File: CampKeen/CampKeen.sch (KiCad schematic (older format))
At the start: 41 parts, among them P1 Digital, P10 CONN_01X01, P11 CONN_01X01, P12 CONN_01X01, P13 CONN_01X01, P2 Power, P3 Analog, P4 Analog, P5 PWM, P6 PWM, P7 Communication, P8 CONN_01X01, P9 CONN_01X01

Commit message: 0.1 version needs to have a power subsystem designed for the AVR and the PCB layout done.
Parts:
- removed Q? (x8): 2N7002, Package_TO_SOT_SMD:SOT-23, symbol Transistor_FET:2N7002
- removed R? (x8): R, symbol Device:R
- added BR1: DF04M, SamacSys_Parts:DIP825W58P510L828H330Q4N, symbol SamacSys_Parts:DF04M
- added C1, C6, C7: 0.1uF, Capacitor_THT:C_Disc_D7.5mm_W5.0mm_P5.00mm, symbol Device:C
- added C10: 1000uF, Capacitor_THT:C_Disc_D7.5mm_W5.0mm_P5.00mm, symbol Device:C
- added C11: 2.2uF, Capacitor_THT:CP_Radial_D4.0mm_P2.00mm, symbol Device:CP
- added C12: 10nF, Capacitor_THT:C_Disc_D7.5mm_W5.0mm_P5.00mm, symbol Device:C
- added C2, C3, C4, C5: 1uF, Capacitor_THT:CP_Radial_D4.0mm_P2.00mm, symbol Device:CP
- added C8: 68uF, Capacitor_THT:CP_Radial_D4.0mm_P2.00mm, symbol Device:CP
- added C9: 120uF, Capacitor_THT:CP_Radial_D4.0mm_P2.00mm, symbol Device:CP
- added D1, D2: 1N5817, SamacSys_Parts:DIOAD1414W86L464D238, symbol SamacSys_Parts:1N5817
- added IC2: TL071CP, SamacSys_Parts:DIP794W53P254L959H508Q8N, symbol SamacSys_Parts:TL071CP
- added IC3: LM2597MX-5.0_NOPB, SamacSys_Parts:SOIC127P600X175-8N, symbol SamacSys_Parts:LM2597MX-5.0_NOPB
- added J1: Tanks, SamacSys_Parts:1727751, symbol SamacSys_Parts:1727751
- added J10: VAC, TerminalBlock_Phoenix:TerminalBlock_Phoenix_MKDS-1,5-2-5.08_1x02_P5.08mm_Horizontal, symbol Connector:Screw_Terminal_01x02
- added J2, J5: IO, SamacSys_Parts:1727751, symbol SamacSys_Parts:1727751
- added J3: Temps, SamacSys_Parts:1727751, symbol SamacSys_Parts:1727751
- added J4: Vin, TerminalBlock_Phoenix:TerminalBlock_Phoenix_MKDS-1,5-2-5.08_1x02_P5.08mm_Horizontal, symbol Connector:Screw_Terminal_01x02
- added J6: GenEnclosure, Connector_PinSocket_2.54mm:PinSocket_1x08_P2.54mm_Vertical, symbol Connector_Generic:Conn_01x08
- added J7: GenHeadL, Connector_PinSocket_2.54mm:PinSocket_1x08_P2.54mm_Vertical, symbol Connector_Generic:Conn_01x08
- added J8: GenHeadR, Connector_PinSocket_2.54mm:PinSocket_1x08_P2.54mm_Vertical, symbol Connector_Generic:Conn_01x08
- added J9: CAC, TerminalBlock_Phoenix:TerminalBlock_Phoenix_MKDS-1,5-2-5.08_1x02_P5.08mm_Horizontal, symbol Connector:Screw_Terminal_01x02
- added K1, K2, K3: DIP05-1A72-12L, SamacSys_Parts:DIP051A7212L, symbol SamacSys_Parts:DIP05-1A72-12L
- added L1: 100mH, Inductor_THT:L_Axial_L9.5mm_D4.0mm_P15.24mm_Horizontal_Fastron_SMCC, symbol Device:L
- added Q1, Q16, Q24, Q6: BC547, Package_TO_SOT_THT:TO-92_Inline, symbol Transistor_BJT:BC547
- added Q10, Q11, Q12, Q13, Q19, Q2, Q20, Q21, Q22, Q23, Q3, Q4, Q5, Q7, Q8, Q9: 2N7000, Package_TO_SOT_THT:TO-92_Inline, symbol Transistor_FET:2N7000
- added Q15, Q17, Q18, Q25: IRF510, SamacSys_Parts:TO254P465X1024X2050-3P, symbol SamacSys_Parts:IRF510
- added R1, R2, R32, R35, R36, R52: 47k, Resistor_THT:R_Axial_DIN0207_L6.3mm_D2.5mm_P7.62mm_Horizontal, symbol Device:R
- added R14, R8: 47K, Resistor_THT:R_Axial_DIN0207_L6.3mm_D2.5mm_P7.62mm_Horizontal, symbol Device:R
- added R15, R16, R3, R33, R34, R4, R47, R48: R, Resistor_THT:R_Axial_DIN0207_L6.3mm_D2.5mm_P7.62mm_Horizontal, symbol Device:R
- added R17, R18, R19, R20, R21, R22, R23, R24, R25, R26, R27, R28, R29, R30, R37, R38, R39, R40, R41, R42, R43, R44, R45, R46: 100k, Resistor_THT:R_Axial_DIN0207_L6.3mm_D2.5mm_P7.62mm_Horizontal, symbol Device:R
- added R49: 10k, Resistor_THT:R_Axial_DIN0207_L6.3mm_D2.5mm_P7.62mm_Horizontal, symbol Device:R
- added R50: 33, Resistor_THT:R_Axial_DIN0207_L6.3mm_D2.5mm_P7.62mm_Horizontal, symbol Device:R
- added R51: 1M, Resistor_THT:R_Axial_DIN0207_L6.3mm_D2.5mm_P7.62mm_Horizontal, symbol Device:R
- added R53, R54: 50, Resistor_THT:R_Axial_DIN0207_L6.3mm_D2.5mm_P7.62mm_Horizontal, symbol Device:R
- added RV1: 500K, Potentiometer_THT:Potentiometer_Bourns_3296W_Vertical, symbol Device:R_POT_US
- added RV10, RV2, RV3, RV4, RV5, RV6, RV7, RV8, RV9: 20k, Potentiometer_THT:Potentiometer_Bourns_3296W_Vertical, symbol Device:R_POT_US
- added RV11: 1M, Potentiometer_THT:Potentiometer_Bourns_3296W_Vertical, symbol Device:R_POT_US
- added U2: TanksVS, SamacSys_Parts:BK_HTC-15M, symbol SamacSys_Parts:BK_HTC-15M
- added U3: MAX232, Package_DIP:DIP-16_W7.62mm_LongPads, symbol Interface_UART:MAX232
- added U4: VS, SamacSys_Parts:BK_HTC-15M, symbol SamacSys_Parts:BK_HTC-15M
- added U5: LPGVS, SamacSys_Parts:BK_HTC-15M, symbol SamacSys_Parts:BK_HTC-15M
- added U6: VAC, SamacSys_Parts:BK_HTC-15M, symbol SamacSys_Parts:BK_HTC-15M
- IC1: renamed from IC?; footprint SOIC127P1032X265-16N -> SamacSys_Parts:SOIC127P1032X265-16N
- Q14: renamed from Q?; footprint TO254P465X1024X2050-3P -> SamacSys_Parts:TO254P465X1024X2050-3P
- R10, R11, R12, R13, R7, R9: renamed from R?; value R -> 100k; footprint (none) -> Resistor_THT:R_Axial_DIN0207_L6.3mm_D2.5mm_P7.62mm_Horizontal
- R31: renamed from R?; value R -> 47k; footprint (none) -> Resistor_THT:R_Axial_DIN0207_L6.3mm_D2.5mm_P7.62mm_Horizontal
- R5, R6: renamed from R?; value R -> 100K; footprint (none) -> Resistor_THT:R_Axial_DIN0207_L6.3mm_D2.5mm_P7.62mm_Horizontal
- U1: renamed from U?; footprint S8411-45R_1 -> SamacSys_Parts:S8411-45R_1
- renumbered P2 to P1, P3 to P2, P4 to P3, P1 to P4
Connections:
- net labels added: +12V, +5P, BathroomPumpLED, BathroomWPS, CLK, CityWaterValveSense, D22, D43, D45, D47, D49, G1-2, G1-4, G3-4, G4-4, GWT12V, GenFuel, KitchenPumpLED, KitchenWPS, LCDBackLight, LCDBacklight, LCDBacklightOut, LPG, LPGSensor, MISO, MOSI, S1-2, S1-4, S3-4, S4-4, ST12V, WarningAlarm, WarningLED, Water, WaterPumpOnSense, d24, d26, d28
- wire segments 177 -> 709
- no-connect marks 7 -> 43
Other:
- moved on the sheet: IC1, Q14, R10, R11, R12, R13, R31, R5, R6, R7, R9, U1

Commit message: 0.1 i think it's ready to be sent off to be fabbed
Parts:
- removed Q19, Q21: 2N7000, Package_TO_SOT_THT:TO-92_Inline, symbol Transistor_FET:2N7000
- removed R37, R38, R41, R42: 100k, Resistor_THT:R_Axial_DIN0207_L6.3mm_D2.5mm_P7.62mm_Horizontal, symbol Device:R
- removed RV2, RV3, RV4, RV5, RV6, RV7, RV8, RV9: 20k, Potentiometer_THT:Potentiometer_Bourns_3296W_Vertical, symbol Device:R_POT_US
- added IC4: TL071CP, SamacSys_Parts:DIP794W53P254L959H508Q8N, symbol SamacSys_Parts:TL071CP
- added J12: IO1, SamacSys_Parts:1727751, symbol SamacSys_Parts:1727751
- added J2: 5VJumper, Connector_PinHeader_2.54mm:PinHeader_1x02_P2.54mm_Vertical, symbol Connector_Generic:Conn_01x02
- added Q20, Q22, Q26, Q27, Q32, Q35: IRF510, SamacSys_Parts:TO254P465X1024X2050-3P, symbol SamacSys_Parts:IRF510
- added Q28, Q29, Q30, Q31, Q33, Q34: 2N7000, Package_TO_SOT_THT:TO-92_Inline, symbol Transistor_FET:2N7000
- added R18: 47K, Resistor_THT:R_Axial_DIN0207_L6.3mm_D2.5mm_P7.62mm_Horizontal, symbol Device:R
- added R44, R45, R48, R49, R63, R68: 47k, Resistor_THT:R_Axial_DIN0207_L6.3mm_D2.5mm_P7.62mm_Horizontal, symbol Device:R
- added R56, R57, R58, R59, R60, R61, R62, R64, R65, R66, R67, R69: 100k, Resistor_THT:R_Axial_DIN0207_L6.3mm_D2.5mm_P7.62mm_Horizontal, symbol Device:R
- added R70, R71, R72, R73, R74, R75, R76, R77: 10k, Resistor_THT:R_Axial_DIN0207_L6.3mm_D2.5mm_P7.62mm_Horizontal, symbol Device:R
- C1: renamed from C6; footprint Capacitor_THT:C_Disc_D7.5mm_W5.0mm_P5.00mm -> Capacitor_THT:C_Rect_L9.0mm_W3.6mm_P7.50mm_MKT
- C10: renamed from C3; footprint Capacitor_THT:CP_Radial_D4.0mm_P2.00mm -> Capacitor_THT:CP_Radial_D5.0mm_P2.50mm
- C11: renamed from C4; footprint Capacitor_THT:CP_Radial_D4.0mm_P2.00mm -> Capacitor_THT:CP_Radial_D5.0mm_P2.50mm
- C12: renamed from C5; footprint Capacitor_THT:CP_Radial_D4.0mm_P2.00mm -> Capacitor_THT:CP_Radial_D5.0mm_P2.50mm
- C2: renamed from C7; footprint Capacitor_THT:C_Disc_D7.5mm_W5.0mm_P5.00mm -> Capacitor_THT:C_Rect_L9.0mm_W3.6mm_P7.50mm_MKT
- C3: renamed from C8; footprint Capacitor_THT:CP_Radial_D4.0mm_P2.00mm -> Capacitor_THT:CP_Radial_D5.0mm_P2.50mm
- C4: renamed from C9; footprint Capacitor_THT:CP_Radial_D4.0mm_P2.00mm -> Capacitor_THT:CP_Radial_D8.0mm_P5.00mm
- C5: renamed from C1; footprint Capacitor_THT:C_Disc_D7.5mm_W5.0mm_P5.00mm -> Capacitor_THT:C_Rect_L9.0mm_W3.6mm_P7.50mm_MKT
- C6: renamed from C10; footprint Capacitor_THT:C_Disc_D7.5mm_W5.0mm_P5.00mm -> Capacitor_THT:C_Rect_L9.0mm_W3.6mm_P7.50mm_MKT
- C9: renamed from C2; footprint Capacitor_THT:CP_Radial_D4.0mm_P2.00mm -> Capacitor_THT:CP_Radial_D5.0mm_P2.50mm
- J7: renamed from J5; value IO -> IO1
- R41: renamed from R53; value 50 -> 47
- R43: renamed from R54; value 50 -> 47
- renumbered C11 to C7, C12 to C8, IC3 to IC1, IC1 to IC2, IC2 to IC3, J4 to J1, J7 to J10, J8 to J11, J9 to J4, J1 to J5, J10 to J6, J2 to J8, J6 to J9, U5 to LPWater1, U4 to Main1, Q25 to Q12, Q12 to Q13, Q13 to Q14, Q16 to Q15, Q14 to Q16, Q15 to Q17, Q17 to Q18, Q18 to Q19, Q20 to Q21, Q22 to Q23, Q23 to Q24, Q24 to Q25, R49 to R1, R9 to R10, R51 to R11, R10 to R12, R50 to R13, R11 to R14, R12 to R15, R13 to R16, R14 to R17, R15 to R19, R1 to R2, R16 to R20, R17 to R21, R18 to R22, R19 to R23, R20 to R24, R21 to R25, R22 to R26, R23 to R27, R24 to R28, R25 to R29, R2 to R3, R26 to R30, R52 to R31, R27 to R32, R28 to R33, R29 to R34, R30 to R35, R33 to R36, R34 to R37, R31 to R38, R32 to R39, R3 to R4, R35 to R40, R36 to R42, R39 to R46, R40 to R47, R4 to R5, R43 to R50, R44 to R51, R45 to R52, R46 to R53, R47 to R54, R48 to R55, R5 to R6, R6 to R7, R7 to R8, R8 to R9, U1 to RTCBattery1, RV11 to RV10, RV10 to RV11, RV1 to RV9, U2 to Tanks1, U3 to U5, U6 to VACFuse1
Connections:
- net +5P: now also J2.1 (Pin_1)
- net +5V: now also IC4.7 (VCC+), J2.2 (Pin_2), Q28.3 (D), Q29.3 (D), Q30.3 (D), Q31.3 (D), Q33.3 (D), Q34.3 (D)
- net 10(**): now also Q28.1 (S), R57.1
- net 11(**): now also Q27.1, R49.1
- net 12(**): now also Q26.1, R48.1
- net 13(**): now also Q22.1, R45.1
- net 24: now also Q35.1, R68.1
- net 37: now also Q32.1, R63.1
- net 41: now also Q20.1, R44.1
- net 5(**): now also Q34.1 (S), R69.1
- net 6(**): now also Q33.1 (S), R66.1
- net 7(**): now also Q31.1 (S), R64.1
- net 8(**): now also Q30.1 (S), R61.1
- net 9(**): now also Q29.1 (S), R59.1
- net A10: now also R76.2
- net A11: now also IC4.2 (IN-), IC4.6 (OUT), R18.2; no longer R11.1, RV10.2
- net A14: now also J12.2
- net A15: now also J12.1
- net A3: now also R70.2
- net A4: now also R71.2
- net A5: now also R72.2
- net A6: now also R73.2
- net A7: now also R74.2
- net A8: now also R77.2
- net A9: now also R75.2
- net GND: now also IC4.4 (VCC-), Q20.3, Q22.3, Q26.3, Q27.3, Q32.3, Q35.3, R18.1, R44.2, R45.2, R48.2, R49.2, R56.2, R57.2, R58.2, R59.2, R60.2, R61.2, R62.2, R63.2, R64.2, R65.2, R66.2, R67.2, R68.2, R69.2, R70.1, R71.1, R72.1, R73.1, R74.1, R75.1, R76.1, R77.1
- net at J8.10: now also Q35.2
- net at J8.12: now also Q32.2
- net 22 renamed AlarmReset
- new net: IC4.3 (IN+), R11.1, RV10.2
- new net: J12.4, Q22.2
- new net: J12.10, Q31.2 (G), R62.1
- new net: J12.11, Q30.2 (G), R60.1
- new net: J12.12, Q29.2 (G), R58.1
- new net: J12.3, Q20.2
- new net: J12.5, Q26.2
- new net: J12.6, Q27.2
- new net: J12.7, Q28.2 (G), R56.1
- new net: J12.8, Q34.2 (G), R67.1
- new net: J12.9, Q33.2 (G), R65.1
- no-connect marks 43 -> 38
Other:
- moved on the sheet: BR1, C7, C8, J6, R11, RV10, VACFuse1

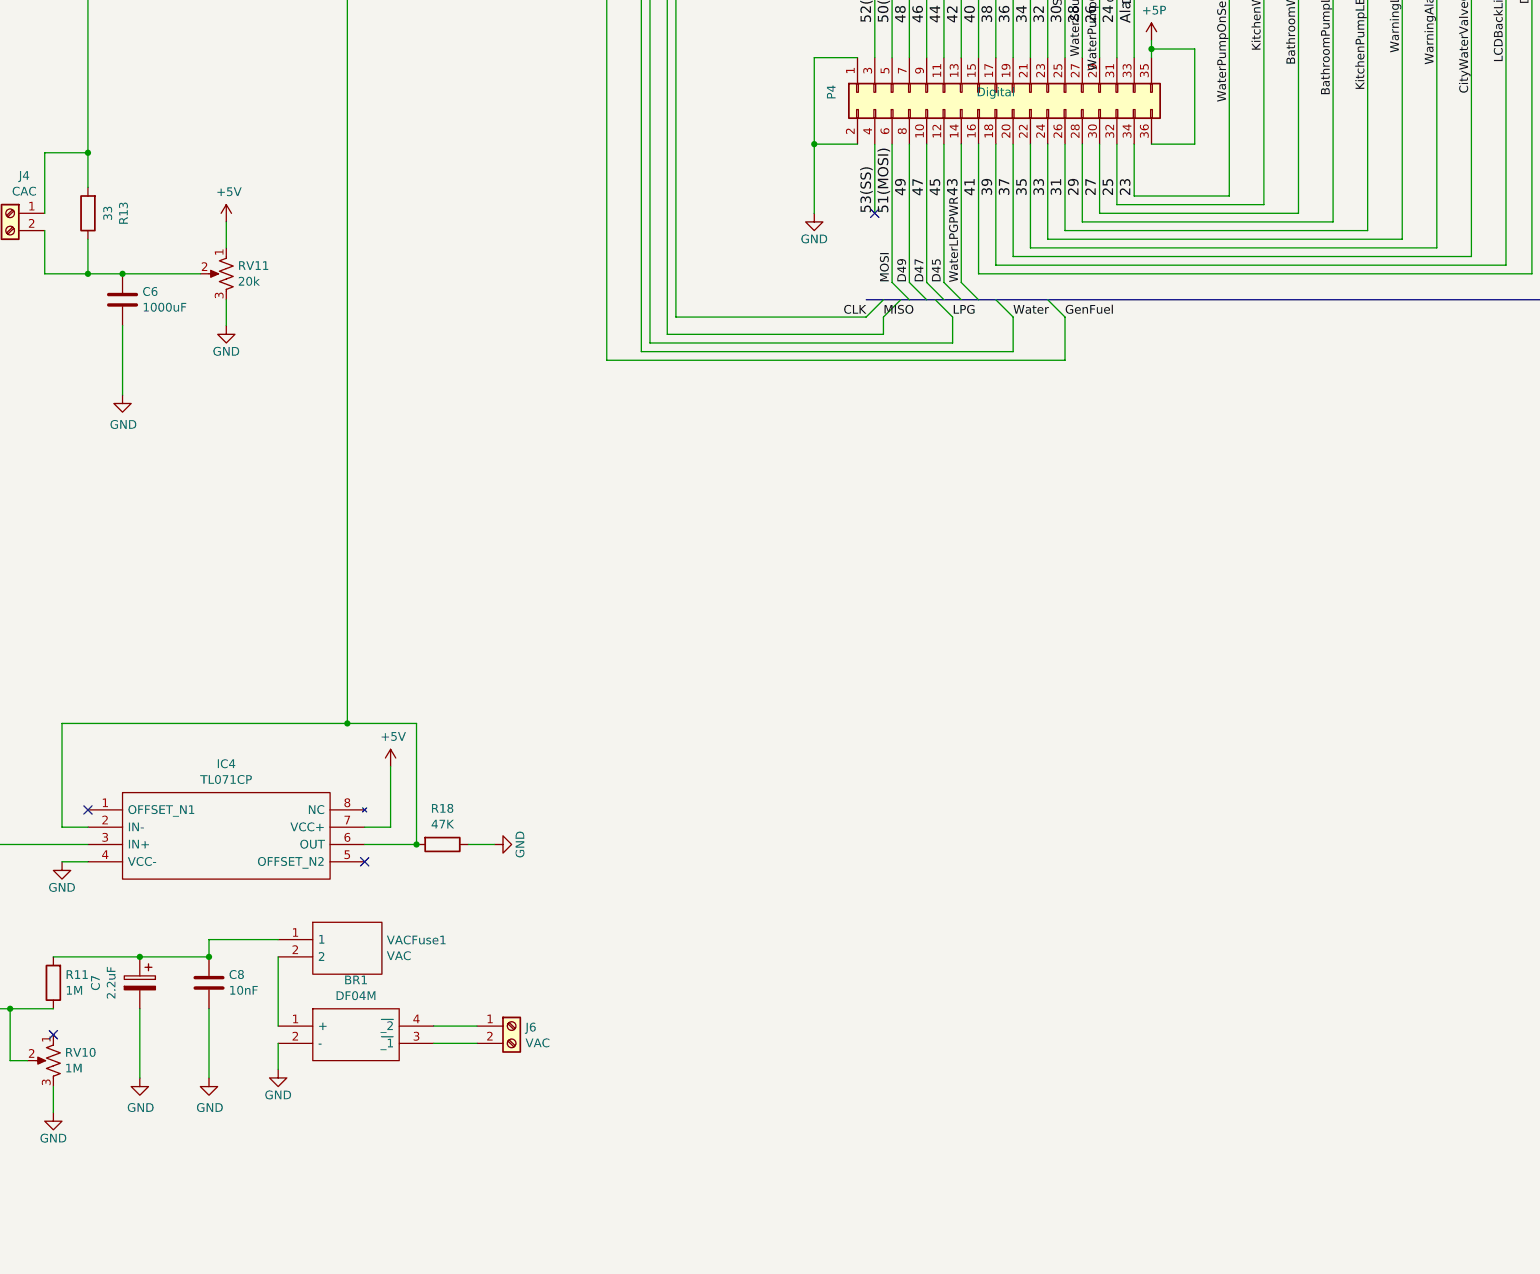
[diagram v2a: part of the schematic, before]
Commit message: WIP that needs to go in it's own branch. it has a few updates like putting the VAC transformer on board and a better voltage reference for the AC current. that still isn't done as it needs a buffer.
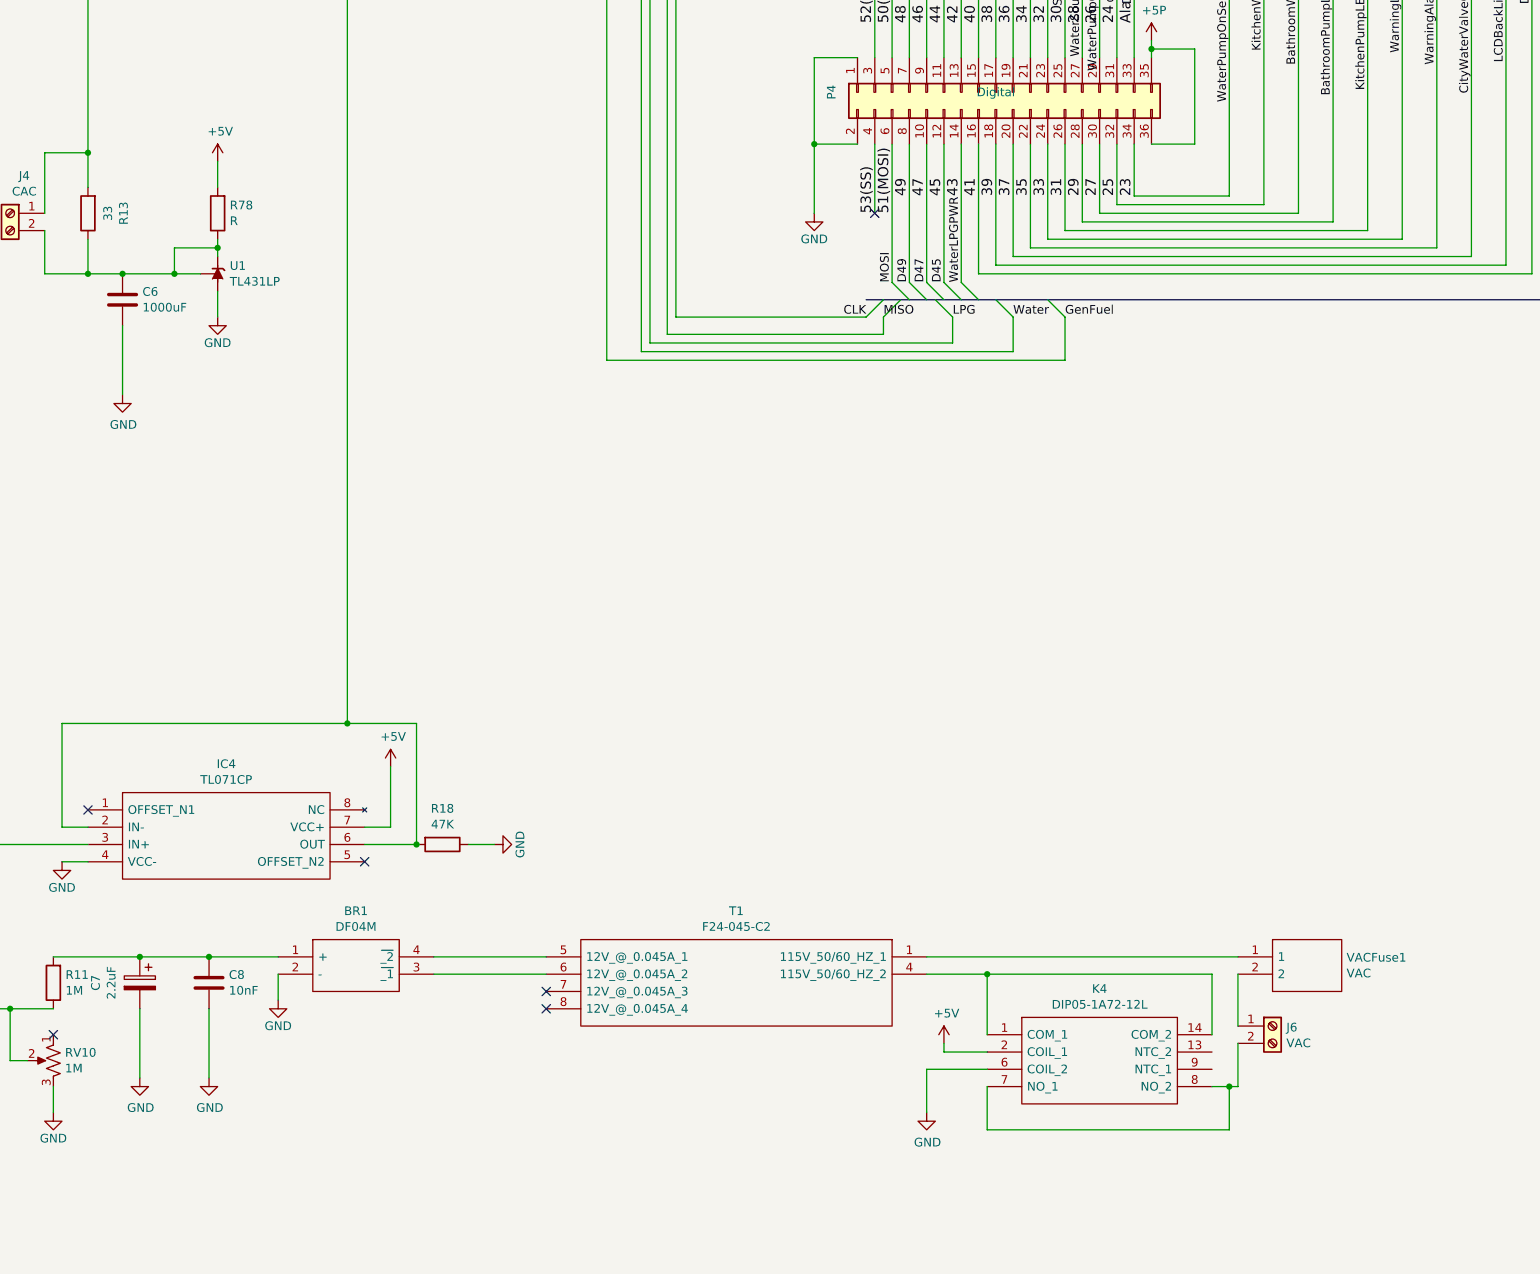
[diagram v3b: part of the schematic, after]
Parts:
- removed RV11: 20k, Potentiometer_THT:Potentiometer_Bourns_3296W_Vertical, symbol Device:R_POT_US
- added K4: DIP05-1A72-12L, SamacSys_Parts:DIP051A7212L, symbol SamacSys_Parts:DIP05-1A72-12L
- added R78: R, Resistor_THT:R_Axial_DIN0207_L6.3mm_D2.5mm_P7.62mm_Horizontal, symbol Device:R
- added T1: F24-045-C2, F24045C2, symbol SamacSys_Parts:F24-045-C2
- added U1: TL431LP, Package_TO_SOT_THT:TO-92_Inline, symbol Reference_Voltage:TL431LP
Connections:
- net +5V: now also K4.2 (COIL_1), R78.2
- net GND: now also K4.6 (COIL_2), U1.2 (A)
- net at BR1.4 (~_2): now also T1.5 (12V_@_0.045A_1); no longer J6.1 (Pin_1)
- net at J6.2 (Pin_2): now also K4.7 (NO_1), K4.8 (NO_2); no longer BR1.3 (~_1)
- net at VACFuse1.2: now also J6.1 (Pin_1); no longer BR1.1 (+)
- net at C7.1, C8.1, R11.2: now also BR1.1 (+); no longer VACFuse1.1
- net at C6.1, J4.2 (Pin_2), R13.1: now also R78.1, U1.1 (REF), U1.3 (K)
- new net: K4.1 (COM_1), K4.14 (COM_2), T1.4 (115V_50/60_HZ_2)
- new net: T1.1 (115V_50/60_HZ_1), VACFuse1.1
- new net: BR1.3 (~_1), T1.6 (12V_@_0.045A_2)
- no-connect marks 38 -> 40
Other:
- moved on the sheet: BR1, J6, VACFuse1
